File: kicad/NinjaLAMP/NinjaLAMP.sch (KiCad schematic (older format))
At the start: 27 parts, among them J1 Barrel_Jack_Switch, J2 Conn_01x05_Male, M1 Fan_3pin, Q1 BSP89, Q2 BSP89, Q3 BSP89, SW1 TACTILE_4, U1 SeeeduinoXIAO

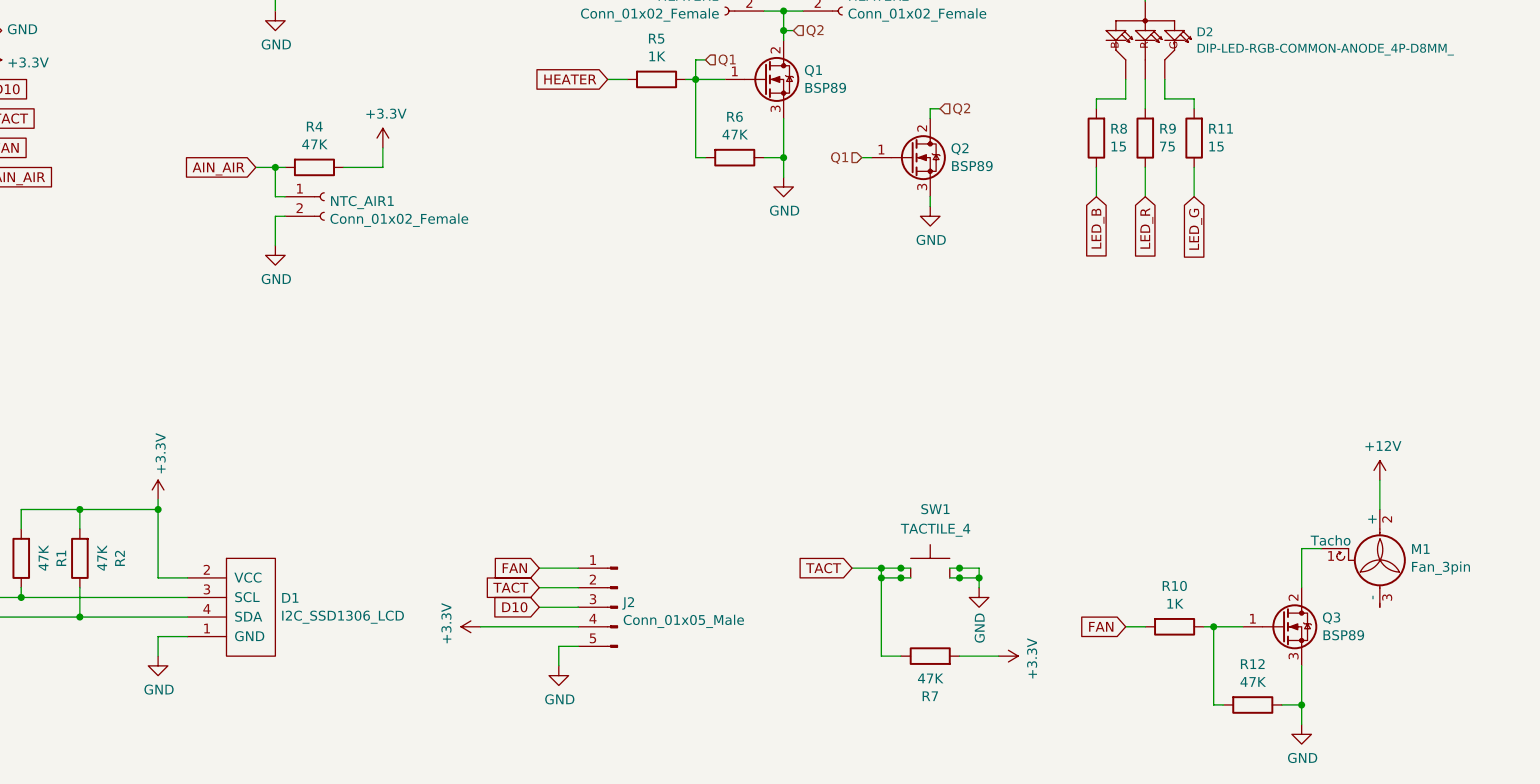
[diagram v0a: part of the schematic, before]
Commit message: pcb ver1.0 complete
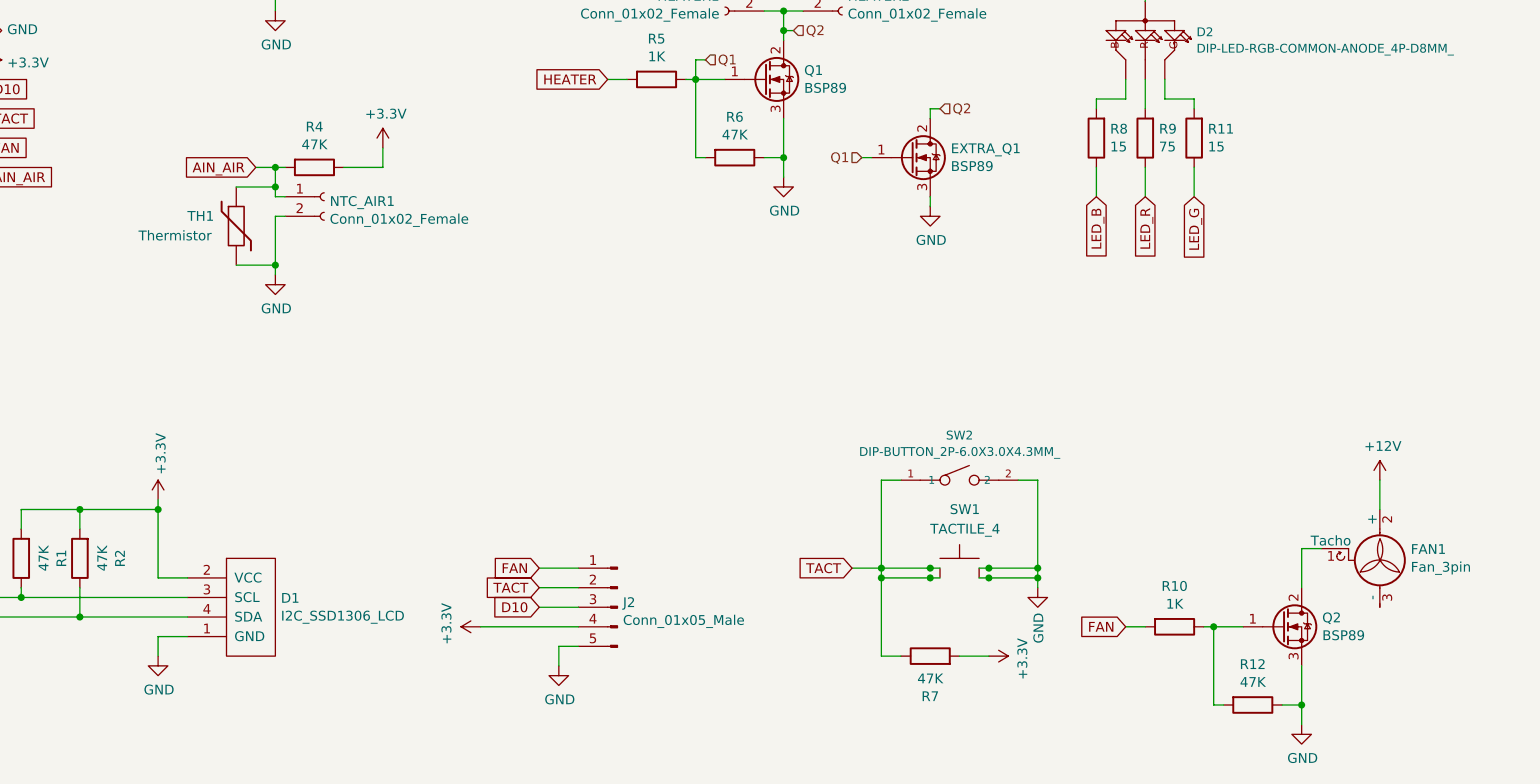
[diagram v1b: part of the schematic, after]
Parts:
- added SW2: DIP-BUTTON_2P-6.0X3.0X4.3MM_, OPL_Switch:SW2-5.0-6.0X3.0X4.3MM, symbol OPL_Switch:DIP-BUTTON_2P-6.0X3.0X4.3MM_
- added TH1: Thermistor, Resistors_SMD:R_0603_HandSoldering, symbol Device:Thermistor
- SW1: footprint Ninja-qPCR:TACTILE_4 -> Ninja-qPCR:SW_TH_Tactile_Omron_B3F-10xx
- renumbered Q2 to EXTRA_Q1, M1 to FAN1, Q3 to Q2
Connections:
- wire segments 120 -> 128
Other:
- moved on the sheet: SW1
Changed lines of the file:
@@
 L power:GND #PWR0105
 U 1 1 5F869CA1
-P 4900 3200
-F 0 "#PWR0105" H 4900 2950 50  0001 C CNN
-F 1 "GND" H 4905 3027 50  0000 C CNN
-F 2 "" H 4900 3200 50  0001 C CNN
-F 3 "" H 4900 3200 50  0001 C CNN
-	1    4900 3200
+P 4900 3350
+F 0 "#PWR0105" H 4900 3100 50  0001 C CNN
+F 1 "GND" H 4905 3177 50  0000 C CNN
+F 2 "" H 4900 3350 50  0001 C CNN
+F 3 "" H 4900 3350 50  0001 C CNN
+	1    4900 3350
 	1    0    0    -1
 $EndComp
@@
 	4950 3050 4900 3050
 Wire Wire Line
-	4900 3050 4900 3200
-Wire Wire Line
 	4950 2800 4900 2800
 Wire Wire Line
 	4950 2950 4900 2950
 Wire Wire Line
-	4900 2950 4900 2800
+	4900 2950 4900 2900
 Connection ~ 4900 2800
 Wire Wire Line
@@
 $EndComp
 $Comp
-L Transistor_FET:BSP89 Q3
+L Transistor_FET:BSP89 Q2
 U 1 1 5F897878
 P 10050 5150
-F 0 "Q3" H 10255 5196 50  0000 L CNN
+F 0 "Q2" H 10255 5196 50  0000 L CNN
 F 1 "BSP89" H 10255 5105 50  0000 L CNN
 F 2 "Ninja-qPCR:SOT95P240X112-3N" H 10250 5075 50  0001 L CIN
@@
 	9250 5150 9350 5150
 $Comp
-L Motor:Fan_3pin M1
+L Motor:Fan_3pin FAN1
 U 1 1 5F8B28BB
 P 10550 4750
-F 0 "M1" H 10708 4746 50  0000 L CNN
+F 0 "FAN1" H 10708 4746 50  0000 L CNN
 F 1 "Fan_3pin" H 10708 4655 50  0000 L CNN
 F 2 "Connectors_Molex:Molex_KK-6410-03_03x2.54mm_Straight" H 10550 4660 50  0001 C CNN
@@
 Connection ~ 7500 2000
 $Comp
-L Transistor_FET:BSP89 Q2
+L Transistor_FET:BSP89 EXTRA_Q1
 U 1 1 5F99BA2C
 P 8150 2750
-F 0 "Q2" H 8355 2796 50  0000 L CNN
+F 0 "EXTRA_Q1" H 8355 2796 50  0000 L CNN
 F 1 "BSP89" H 8355 2705 50  0000 L CNN
 F 2 "TO_SOT_Packages_THT:TO-220-3_Vertical" H 8350 2675 50  0001 L CIN
@@
 L Ninja-qPCR:TACTILE_4 SW1
 U 1 1 5F9E21A3
-P 8250 4850
-F 0 "SW1" H 8200 5150 50  0000 L CNN
-F 1 "TACTILE_4" H 8100 5050 50  0000 L CNN
-F 2 "Ninja-qPCR:TACTILE_4" H 8250 5050 50  0001 C CNN
-F 3 "http://www.apem.com/int/index.php?controller=attachment&id_attachment=488" H 8250 5050 50  0001 C CNN
-	1    8250 4850
+P 8400 4850
+F 0 "SW1" H 8350 5150 50  0000 L CNN
+F 1 "TACTILE_4" H 8250 5050 50  0000 L CNN
+F 2 "Ninja-qPCR:SW_TH_Tactile_Omron_B3F-10xx" H 8400 5050 50  0001 C CNN
+F 3 "http://www.apem.com/int/index.php?controller=attachment&id_attachment=488" H 8400 5050 50  0001 C CNN
+	1    8400 4850
 	1    0    0    -1
 $EndComp
@@
 L power:GND #PWR0120
 U 1 1 5F9E3621
-P 8500 4950
-F 0 "#PWR0120" H 8500 4700 50  0001 C CNN
-F 1 "GND" V 8505 4822 50  0000 R CNN
-F 2 "" H 8500 4950 50  0001 C CNN
-F 3 "" H 8500 4950 50  0001 C CNN
-	1    8500 4950
-	1    0    0    -1
-$EndComp
-Wire Wire Line
-	8350 4850 8400 4850
-Wire Wire Line
-	8500 4850 8500 4900
-Connection ~ 8400 4850
-Wire Wire Line
-	8400 4850 8500 4850
-Wire Wire Line
-	8350 4900 8400 4900
-Connection ~ 8500 4900
-Wire Wire Line
-	8500 4900 8500 4950
-Connection ~ 8400 4900
-Wire Wire Line
-	8400 4900 8500 4900
+P 8800 4950
+F 0 "#PWR0120" H 8800 4700 50  0001 C CNN
+F 1 "GND" V 8805 4822 50  0000 R CNN
+F 2 "" H 8800 4950 50  0001 C CNN
+F 3 "" H 8800 4950 50  0001 C CNN
+	1    8800 4950
+	1    0    0    -1
+$EndComp
+Wire Wire Line
+	8800 4850 8800 4900
+Connection ~ 8800 4900
+Wire Wire Line
+	8800 4900 8800 4950
 $Comp
 L Device:R R7
@@
 L power:+3.3V #PWR0121
 U 1 1 5F9F64BE
-P 8600 5300
-F 0 "#PWR0121" H 8600 5150 50  0001 C CNN
-F 1 "+3.3V" H 8615 5473 50  0000 C CNN
-F 2 "" H 8600 5300 50  0001 C CNN
-F 3 "" H 8600 5300 50  0001 C CNN
-	1    8600 5300
+P 8550 5300
+F 0 "#PWR0121" H 8550 5150 50  0001 C CNN
+F 1 "+3.3V" H 8565 5473 50  0000 C CNN
+F 2 "" H 8550 5300 50  0001 C CNN
+F 3 "" H 8550 5300 50  0001 C CNN
+	1    8550 5300
 	0    1    1    0
 $EndComp
 Wire Wire Line
-	8400 5300 8600 5300
-Wire Wire Line
-	8150 4850 8100 4850
-Wire Wire Line
-	8000 4850 8000 4900
+	8300 4850 8250 4850
 Wire Wire Line
 	8000 5300 8100 5300
-Connection ~ 8100 4850
-Wire Wire Line
-	8100 4850 8000 4850
-Wire Wire Line
-	8150 4900 8100 4900
-Connection ~ 8000 4900
-Wire Wire Line
-	8000 4900 8000 5300
-Connection ~ 8100 4900
-Wire Wire Line
-	8100 4900 8000 4900
+Connection ~ 8250 4850
+Wire Wire Line
+	8300 4900 8250 4900
+Connection ~ 8250 4900
 Text GLabel 7850 4850 0    50   Input ~ 0
 TACT
@@
 	0    1    1    0
 $EndComp
+Wire Wire Line
+	4900 2900 4700 2900
+Connection ~ 4900 2900
+Wire Wire Line
+	4900 2900 4900 2800
+Wire Wire Line
+	4900 3050 4900 3300
+Wire Wire Line
+	4700 3300 4900 3300
+Connection ~ 4900 3300
+Wire Wire Line
+	4900 3300 4900 3350
+$Comp
+L Device:Thermistor TH1
+U 1 1 5FAA0CD9
+P 4700 3100
+F 0 "TH1" H 4450 3150 50  0000 L CNN
+F 1 "Thermistor" H 4200 3050 50  0000 L CNN
+F 2 "Resistors_SMD:R_0603_HandSoldering" H 4700 3100 50  0001 C CNN
+F 3 "~" H 4700 3100 50  0001 C CNN
+	1    4700 3100
+	1    0    0    -1
+$EndComp
+$Comp
+L OPL_Switch:DIP-BUTTON_2P-6.0X3.0X4.3MM_ SW2
+U 1 1 5FAE64FD
+P 8400 4400
+F 0 "SW2" H 8400 4629 45  0000 C CNN
+F 1 "DIP-BUTTON_2P-6.0X3.0X4.3MM_" H 8400 4545 45  0000 C CNN
+F 2 "OPL_Switch:SW2-5.0-6.0X3.0X4.3MM" H 8400 4400 50  0001 C CNN
+F 3 "" H 8400 4400 50  0001 C CNN
+F 4 "TS-1101F" H 8430 4550 20  0001 C CNN "MPN"
+F 5 "311020025" H 8430 4550 20  0001 C CNN "SKU"
+	1    8400 4400
+	1    0    0    -1
+$EndComp
+Wire Wire Line
+	8100 4400 8000 4400
+Wire Wire Line
+	8000 4400 8000 4850
+Wire Wire Line
+	8000 4850 8000 4900
+Wire Wire Line
+	8000 4850 8250 4850
+Wire Wire Line
+	8000 4900 8250 4900
+Connection ~ 8000 4900
+Wire Wire Line
+	8000 4900 8000 5300
+Wire Wire Line
+	8500 4850 8550 4850
+Connection ~ 8550 4850
+Wire Wire Line
+	8550 4850 8800 4850
+Wire Wire Line
+	8500 4900 8550 4900
+Connection ~ 8550 4900
+Wire Wire Line
+	8550 4900 8800 4900
+Wire Wire Line
+	8700 4400 8800 4400
+Wire Wire Line
+	8800 4400 8800 4850
+Connection ~ 8800 4850
+Wire Wire Line
+	8400 5300 8550 5300
 $EndSCHEMATC

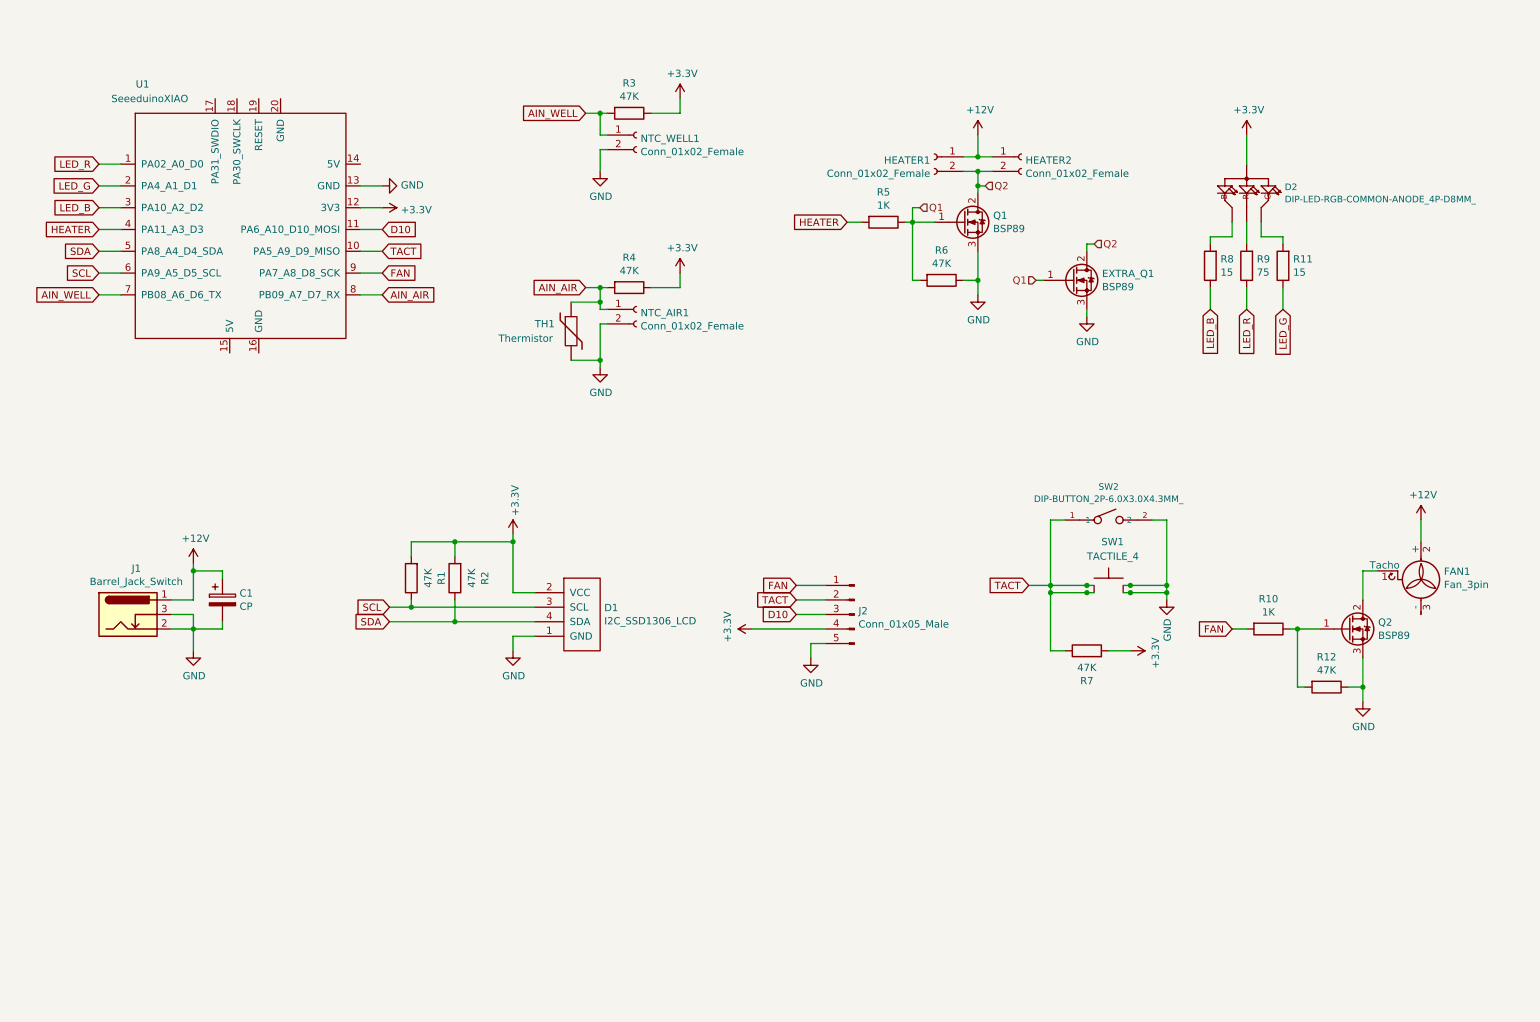
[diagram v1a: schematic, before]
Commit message: pcb ver1.0 complete
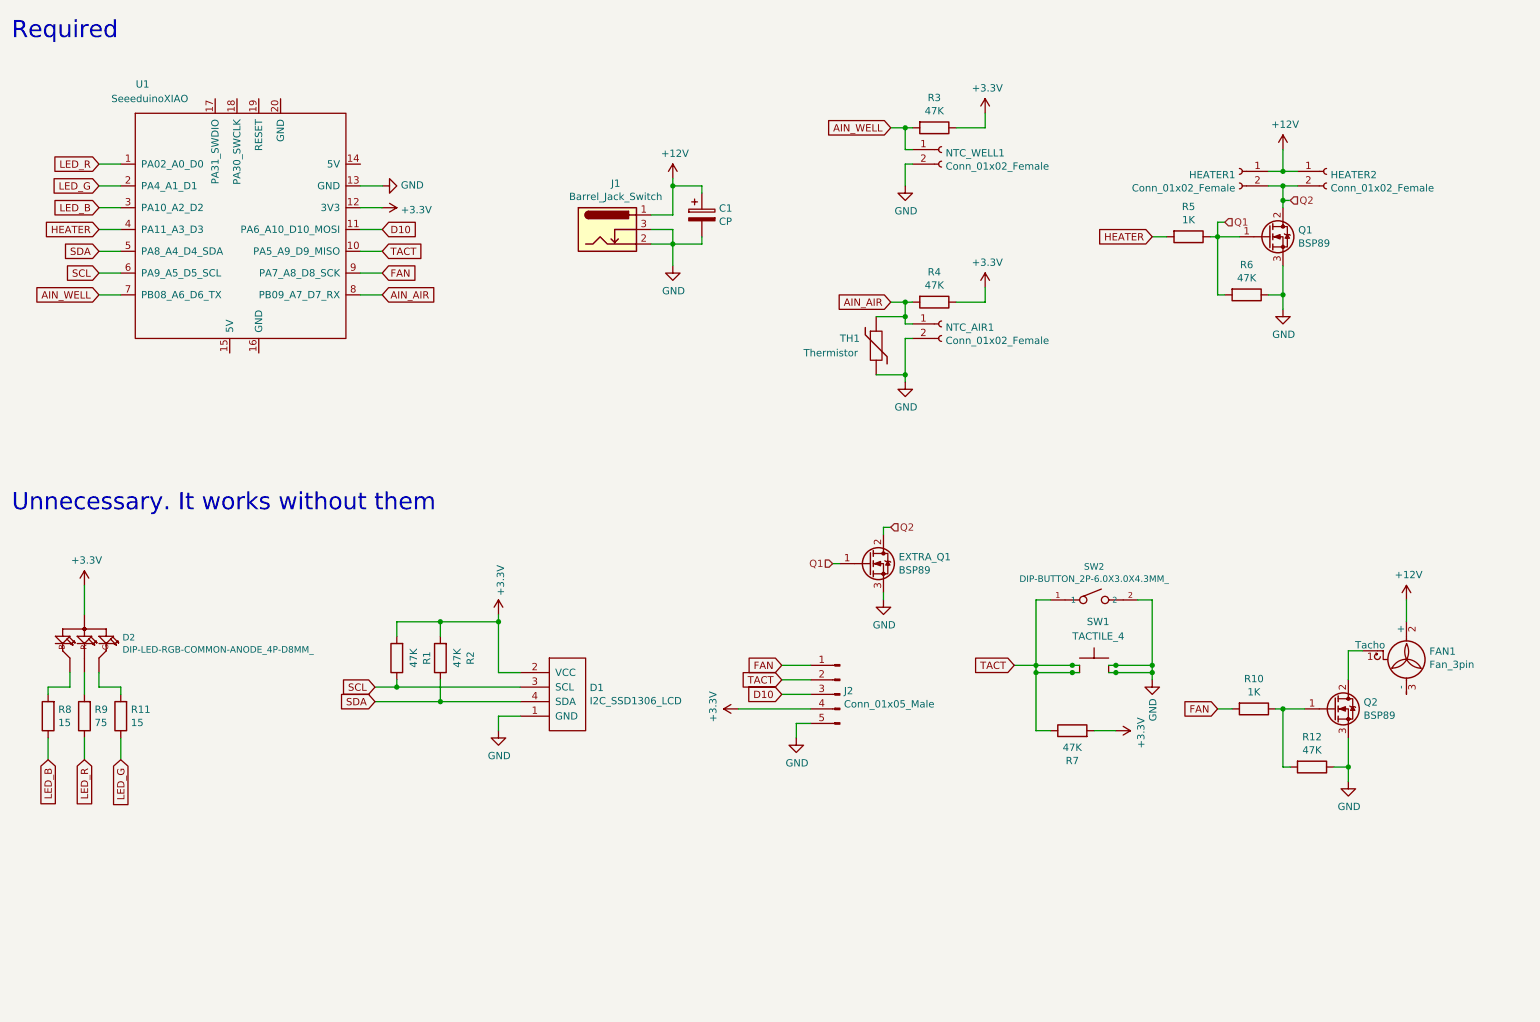
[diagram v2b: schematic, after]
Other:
- note added: "Required"
- note added: "Unnecessary. It works without them"
- moved on the sheet: C1, D1, D2, EXTRA_Q1, FAN1, HEATER1, HEATER2, J1, J2, NTC_AIR1, NTC_WELL1, Q1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

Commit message: added tacts and EEPROM
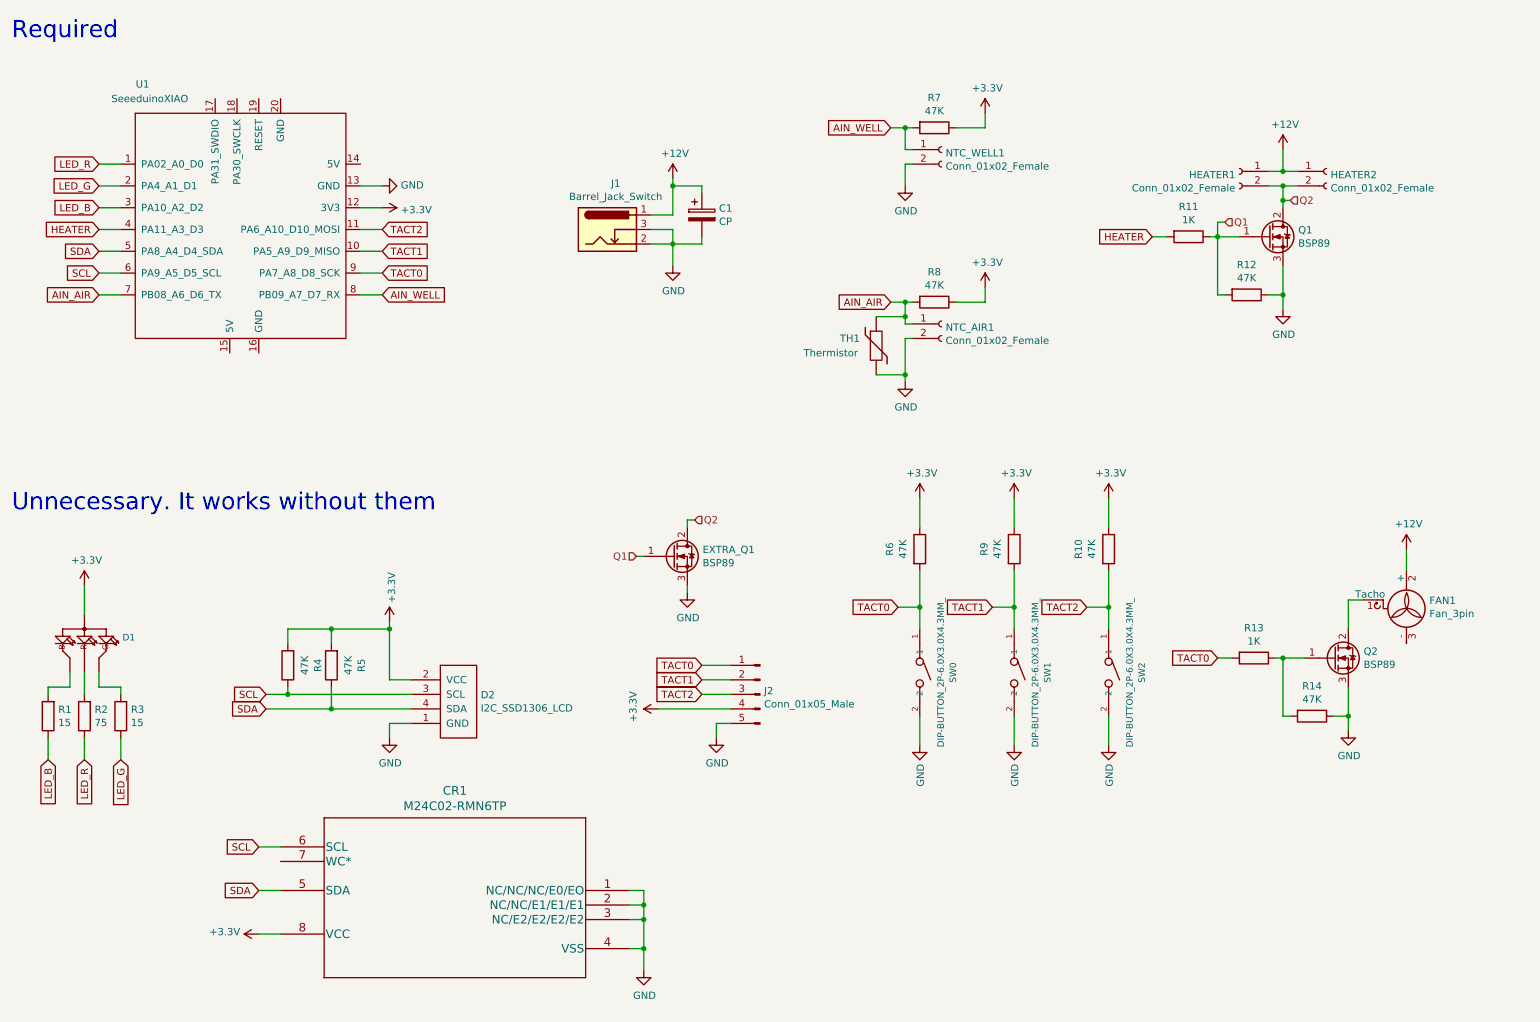
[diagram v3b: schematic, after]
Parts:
- removed SW1: TACTILE_4, Ninja-qPCR:SW_TH_Tactile_Omron_B3F-10xx, symbol Ninja-qPCR:TACTILE_4
- added CR1: M24C02-RMN6TP, Ninja-qPCR:M24C02-RMN6TP, symbol Ninja-qPCR:M24C02-RMN6TP
- added R10, R6: 47K, Resistors_SMD:R_0603_HandSoldering, symbol Device:R
- added SW0, SW2: DIP-BUTTON_2P-6.0X3.0X4.3MM_, OPL_Switch:SW2-5.0-6.0X3.0X4.3MM, symbol OPL_Switch:DIP-BUTTON_2P-6.0X3.0X4.3MM_
- renumbered D2 to D1, D1 to D2, R8 to R1, R5 to R11, R6 to R12, R10 to R13, R12 to R14, R9 to R2, R11 to R3, R1 to R4, R2 to R5, R3 to R7, R4 to R8, R7 to R9, SW2 to SW1
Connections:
- net labels added: TACT0, TACT1, TACT2
- net labels removed: D10, FAN, TACT
- wire segments 128 -> 135
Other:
- moved on the sheet: D2, EXTRA_Q1, FAN1, J2, Q2, R13, R14, R4, R5, R9, SW1
